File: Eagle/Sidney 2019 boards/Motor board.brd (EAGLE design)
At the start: 110 x 122 mm, 43 parts, among them IC2 LM2940CS-5.0_NOPB, IC3 LM3940IS-3.3

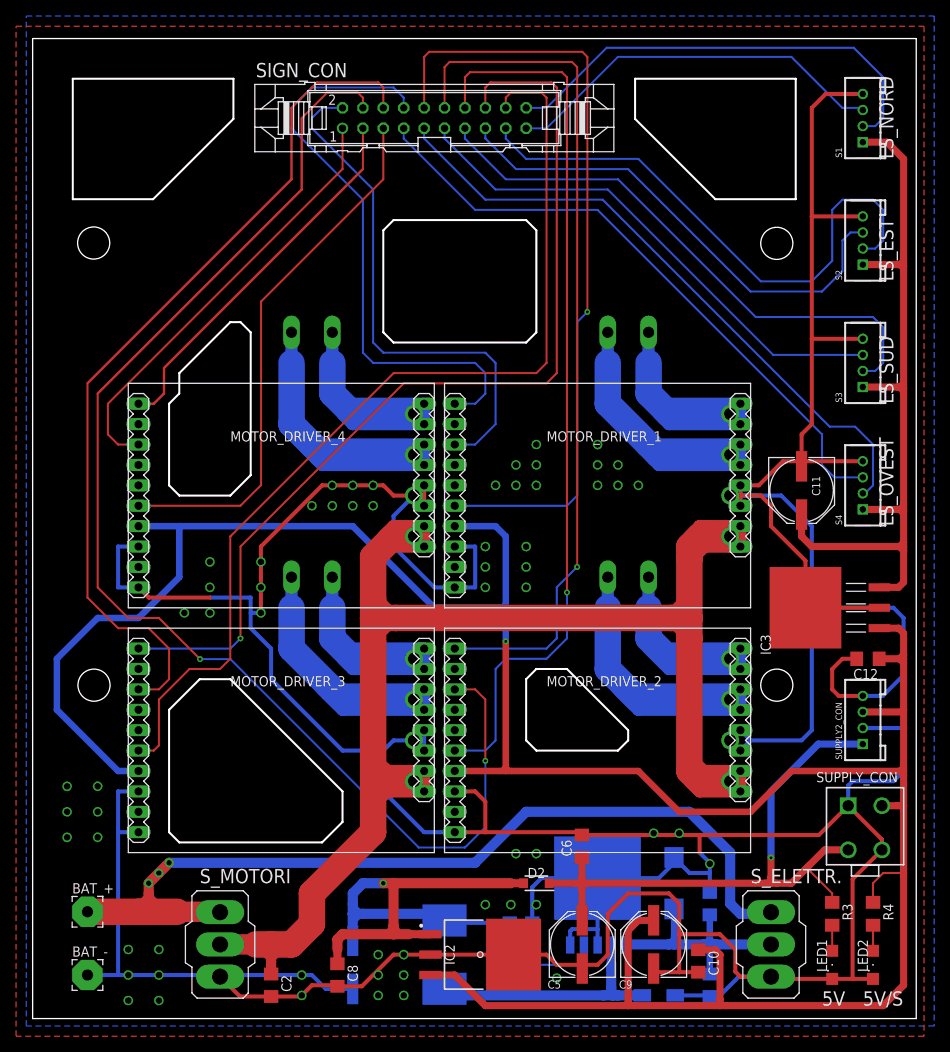
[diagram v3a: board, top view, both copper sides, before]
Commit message: Fixed motor driver pin hardly connected to ground
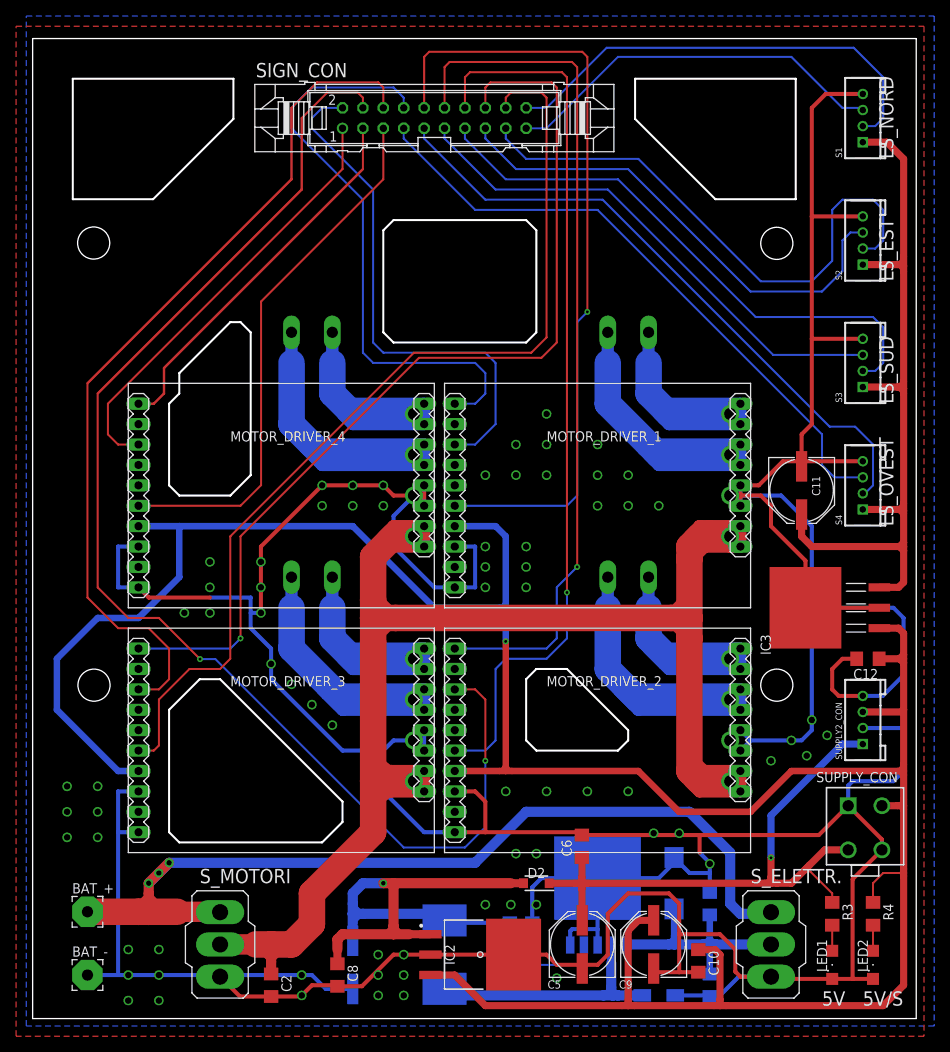
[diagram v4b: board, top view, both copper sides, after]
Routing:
- net M3_INB: track 123.0 -> 121.1 mm
- net +5V: track 85.8 -> 84.0 mm
- net M3_INA: track 120.5 -> 119.0 mm
- net GND: vias 61 -> 73
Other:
- outline, holes or cut-outs redrawn
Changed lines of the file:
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@@
 <wire x1="48.26" y1="74.93" x2="66.04" y2="74.93" width="0.254" layer="20"/>
 <wire x1="66.04" y1="74.93" x2="68.58" y2="77.47" width="0.254" layer="20"/>
-<wire x1="68.58" y1="77.47" x2="68.58" y2="81.28" width="0.254" layer="20"/>
-<wire x1="54.61" y1="95.25" x2="50.8" y2="95.25" width="0.254" layer="20"/>
+<wire x1="68.58" y1="77.47" x2="68.58" y2="80.01" width="0.254" layer="20"/>
+<wire x1="53.34" y1="95.25" x2="50.8" y2="95.25" width="0.254" layer="20"/>
 <wire x1="50.8" y1="95.25" x2="46.99" y2="91.44" width="0.254" layer="20"/>
 <wire x1="91.44" y1="95.25" x2="92.71" y2="96.52" width="0.254" layer="20"/>
@@
 <wire x1="46.99" y1="129.54" x2="46.99" y2="119.38" width="0.254" layer="20"/>
 <wire x1="46.99" y1="119.38" x2="48.26" y2="118.11" width="0.254" layer="20"/>
-<wire x1="54.61" y1="95.25" x2="68.58" y2="81.28" width="0.254" layer="20"/>
+<wire x1="53.34" y1="95.25" x2="68.58" y2="80.01" width="0.254" layer="20"/>
 </plain>
 <attributes>
@@
 <wire x1="43.18" y1="106.68" x2="44.45" y2="105.41" width="0.508" layer="1"/>
 <wire x1="58.42" y1="111.76" x2="66.04" y2="119.38" width="0.508" layer="1"/>
-<wire x1="66.04" y1="119.38" x2="67.31" y2="119.38" width="0.508" layer="1"/>
-<wire x1="69.85" y1="119.38" x2="67.31" y2="119.38" width="0.508" layer="1"/>
+<wire x1="69.85" y1="119.38" x2="66.04" y2="119.38" width="0.508" layer="1"/>
 <wire x1="77.47" y1="118.11" x2="78.74" y2="119.38" width="0.508" layer="1"/>
 <wire x1="78.74" y1="119.38" x2="78.74" y2="116.84" width="0.508" layer="1"/>
@@
 <via x="58.42" y="109.855" extent="1-16" drill="0.8"/>
 <via x="58.42" y="103.505" extent="1-16" drill="0.8"/>
-<via x="64.77" y="116.84" extent="1-16" drill="0.8"/>
-<via x="67.31" y="116.84" extent="1-16" drill="0.8"/>
+<via x="66.04" y="116.84" extent="1-16" drill="0.8"/>
 <via x="69.85" y="116.84" extent="1-16" drill="0.8"/>
-<via x="67.31" y="119.38" extent="1-16" drill="0.8"/>
+<via x="66.04" y="119.38" extent="1-16" drill="0.8"/>
 <via x="69.85" y="119.38" extent="1-16" drill="0.8"/>
-<via x="72.39" y="119.38" extent="1-16" drill="0.8"/>
+<via x="73.66" y="119.38" extent="1-16" drill="0.8"/>
 <wire x1="132.585" y1="97.79" x2="130.81" y2="97.79" width="0.508" layer="1"/>
 <wire x1="130.81" y1="97.79" x2="129.54" y2="96.52" width="0.508" layer="1"/>
@@
 <wire x1="100.33" y1="59.69" x2="101.6" y2="60.96" width="0.508" layer="1"/>
 <wire x1="101.6" y1="60.96" x2="101.6" y2="66.04" width="0.508" layer="1"/>
-<via x="90.17" y="119.38" extent="1-16" drill="0.8"/>
-<via x="87.63" y="119.38" extent="1-16" drill="0.8"/>
-<via x="92.71" y="119.38" extent="1-16" drill="0.8"/>
-<via x="90.17" y="121.92" extent="1-16" drill="0.8"/>
-<via x="92.71" y="121.92" extent="1-16" drill="0.8"/>
-<via x="92.71" y="124.46" extent="1-16" drill="0.8"/>
-<via x="105.41" y="119.38" extent="1-16" drill="0.8"/>
-<via x="102.87" y="119.38" extent="1-16" drill="0.8"/>
-<via x="100.33" y="119.38" extent="1-16" drill="0.8"/>
-<via x="100.33" y="121.92" extent="1-16" drill="0.8"/>
+<via x="90.17" y="124.46" extent="1-16" drill="0.8"/>
+<via x="86.36" y="120.65" extent="1-16" drill="0.8"/>
+<via x="93.98" y="120.65" extent="1-16" drill="0.8"/>
+<via x="90.17" y="120.65" extent="1-16" drill="0.8"/>
+<via x="93.98" y="128.27" extent="1-16" drill="0.8"/>
+<via x="93.98" y="124.46" extent="1-16" drill="0.8"/>
+<via x="107.95" y="116.84" extent="1-16" drill="0.8"/>
+<via x="104.14" y="116.84" extent="1-16" drill="0.8"/>
+<via x="100.33" y="116.84" extent="1-16" drill="0.8"/>
+<via x="100.33" y="120.65" extent="1-16" drill="0.8"/>
 <via x="100.33" y="124.46" extent="1-16" drill="0.8"/>
-<via x="102.87" y="121.92" extent="1-16" drill="0.8"/>
-<via x="72.39" y="116.84" extent="1-16" drill="0.8"/>
+<via x="104.14" y="120.65" extent="1-16" drill="0.8"/>
+<via x="73.66" y="116.84" extent="1-16" drill="0.8"/>
 <wire x1="125.73" y1="125.73" x2="125.73" y2="122.428" width="0.508" layer="1"/>
 <wire x1="125.73" y1="122.428" x2="125.778" y2="122.38" width="0.508" layer="1"/>
@@
 <via x="91.44" y="109.22" extent="1-16" drill="0.8"/>
 <via x="91.44" y="106.68" extent="1-16" drill="0.8"/>
-<wire x1="69.85" y1="119.38" x2="72.39" y2="119.38" width="0.508" layer="1"/>
-<wire x1="72.39" y1="119.38" x2="73.66" y2="119.38" width="0.508" layer="1"/>
+<wire x1="69.85" y1="119.38" x2="73.66" y2="119.38" width="0.508" layer="1"/>
 <wire x1="73.66" y1="119.38" x2="74.93" y2="118.11" width="0.508" layer="1"/>
 <wire x1="74.93" y1="118.11" x2="77.47" y2="118.11" width="0.508" layer="1"/>
@@
 <via x="107.315" y="76.073" extent="1-16" drill="0.8"/>
 <via x="110.49" y="76.073" extent="1-16" drill="0.8"/>
+<via x="67.31" y="89.535" extent="1-16" drill="0.8"/>
+<via x="64.77" y="92.075" extent="1-16" drill="0.8"/>
+<via x="62.23" y="94.615" extent="1-16" drill="0.8"/>
+<via x="59.69" y="97.155" extent="1-16" drill="0.8"/>
+<via x="88.9" y="81.28" extent="1-16" drill="0.8"/>
+<via x="93.98" y="81.28" extent="1-16" drill="0.8"/>
+<via x="99.06" y="81.28" extent="1-16" drill="0.8"/>
+<via x="104.14" y="81.28" extent="1-16" drill="0.8"/>
+<via x="121.92" y="85.09" extent="1-16" drill="0.8"/>
+<via x="124.46" y="87.63" extent="1-16" drill="0.8"/>
+<via x="127" y="90.17" extent="1-16" drill="0.8"/>
+<via x="126.365" y="85.725" extent="1-16" drill="0.8"/>
+<via x="128.905" y="88.265" extent="1-16" drill="0.8"/>
 </signal>
 <signal name="+5V">
@@
 <wire x1="97.61941875" y1="69.85" x2="98.38141875" y2="70.612" width="0.3048" layer="1"/>
 <contactref element="SUPPLY2_CON" pad="1"/>
-<wire x1="133.35" y1="87.17" x2="127.81" y2="87.17" width="0.889" layer="16"/>
-<wire x1="121.92" y1="81.28" x2="121.92" y2="73.025" width="0.889" layer="16"/>
+<wire x1="133.35" y1="87.17" x2="130.81" y2="87.17" width="0.889" layer="16"/>
 <via x="121.92" y="73.025" extent="1-16" drill="0.35"/>
 <wire x1="121.92" y1="73.025" x2="121.92" y2="70.612" width="0.889" layer="1"/>
@@
 <wire x1="121.158" y1="69.85" x2="121.92" y2="70.612" width="0.4064" layer="1"/>
 <wire x1="121.92" y1="70.612" x2="122.682" y2="69.85" width="0.4064" layer="1"/>
-<wire x1="127.81" y1="87.17" x2="121.92" y2="81.28" width="0.889" layer="16"/>
+<wire x1="130.81" y1="87.17" x2="121.92" y2="78.28" width="0.889" layer="16"/>
+<wire x1="121.92" y1="78.28" x2="121.92" y2="73.025" width="0.889" layer="16"/>
 </signal>
 <signal name="N$6">
@@
 <wire x1="63.5" y1="165.1" x2="63.5" y2="156.21" width="0.3048" layer="1"/>
 <wire x1="63.5" y1="156.21" x2="38.1" y2="130.81" width="0.3048" layer="1"/>
-<wire x1="50.84" y1="97.75" x2="54.61" y2="97.75" width="0.254" layer="16"/>
-<wire x1="54.61" y1="97.75" x2="78.065" y2="74.295" width="0.254" layer="16"/>
-<wire x1="78.065" y1="74.295" x2="83.82" y2="74.295" width="0.254" layer="16"/>
+<wire x1="50.84" y1="97.75" x2="52.745" y2="97.75" width="0.254" layer="16"/>
+<wire x1="76.2" y1="74.295" x2="83.82" y2="74.295" width="0.254" layer="16"/>
+<wire x1="76.2" y1="74.295" x2="52.745" y2="97.75" width="0.254" layer="16"/>
 </signal>
 <signal name="M2_INA">
@@
 <wire x1="86.36" y1="166.37" x2="86.36" y2="168.91" width="0.254" layer="1"/>
 <wire x1="86.36" y1="168.91" x2="86.995" y2="169.545" width="0.254" layer="1"/>
-<wire x1="55.88" y1="111.76" x2="55.88" y2="100.33" width="0.254" layer="1"/>
 <via x="55.88" y="100.33" extent="1-16" drill="0.35"/>
 <wire x1="55.88" y1="100.33" x2="54.61" y2="99.06" width="0.254" layer="16"/>
-<wire x1="76.2" y1="132.08" x2="55.88" y2="111.76" width="0.254" layer="1"/>
-<wire x1="95.25" y1="133.35" x2="93.98" y2="132.08" width="0.254" layer="1"/>
-<wire x1="93.98" y1="132.08" x2="76.2" y2="132.08" width="0.254" layer="1"/>
-<wire x1="95.25" y1="168.91" x2="95.25" y2="133.35" width="0.254" layer="1"/>
+<wire x1="95.25" y1="168.91" x2="95.25" y2="137.16" width="0.254" layer="1"/>
+<wire x1="95.25" y1="137.16" x2="93.345" y2="135.255" width="0.254" layer="1"/>
+<wire x1="93.345" y1="135.255" x2="78.105" y2="135.255" width="0.254" layer="1"/>
+<wire x1="78.105" y1="135.255" x2="55.88" y2="113.03" width="0.254" layer="1"/>
+<wire x1="55.88" y1="113.03" x2="55.88" y2="100.33" width="0.254" layer="1"/>
 </signal>
 <signal name="M3_INB">
@@
 <wire x1="93.98" y1="167.64" x2="93.345" y2="168.275" width="0.254" layer="1"/>
 <wire x1="89.535" y1="168.275" x2="93.345" y2="168.275" width="0.254" layer="1"/>
-<wire x1="44.45" y1="86.36" x2="43.18" y2="86.36" width="0.254" layer="1"/>
-<wire x1="54.61" y1="113.03" x2="74.93" y2="133.35" width="0.254" layer="1"/>
-<wire x1="54.61" y1="113.03" x2="54.61" y2="97.79" width="0.254" layer="1"/>
-<wire x1="74.93" y1="133.35" x2="92.71" y2="133.35" width="0.254" layer="1"/>
-<wire x1="92.71" y1="133.35" x2="93.98" y2="134.62" width="0.254" layer="1"/>
-<wire x1="93.98" y1="134.62" x2="93.98" y2="167.64" width="0.254" layer="1"/>
+<wire x1="45.085" y1="86.36" x2="43.18" y2="86.36" width="0.254" layer="1"/>
+<wire x1="54.61" y1="97.79" x2="54.61" y2="113.03" width="0.254" layer="1"/>
+<wire x1="93.98" y1="137.795" x2="93.98" y2="167.64" width="0.254" layer="1"/>
 <wire x1="54.61" y1="97.79" x2="53.34" y2="96.52" width="0.254" layer="1"/>
 <wire x1="53.34" y1="96.52" x2="49.53" y2="96.52" width="0.254" layer="1"/>
 <wire x1="49.53" y1="96.52" x2="45.72" y2="92.71" width="0.254" layer="1"/>
 <wire x1="45.72" y1="86.995" x2="45.085" y2="86.36" width="0.254" layer="1"/>
-<wire x1="45.085" y1="86.36" x2="44.45" y2="86.36" width="0.254" layer="1"/>
 <wire x1="45.72" y1="92.71" x2="45.72" y2="86.995" width="0.254" layer="1"/>
+<wire x1="92.075" y1="135.89" x2="93.98" y2="137.795" width="0.254" layer="1"/>
+<wire x1="54.61" y1="113.03" x2="77.47" y2="135.89" width="0.254" layer="1"/>
+<wire x1="77.47" y1="135.89" x2="92.075" y2="135.89" width="0.254" layer="1"/>
 </signal>
 <signal name="M4_PWM">

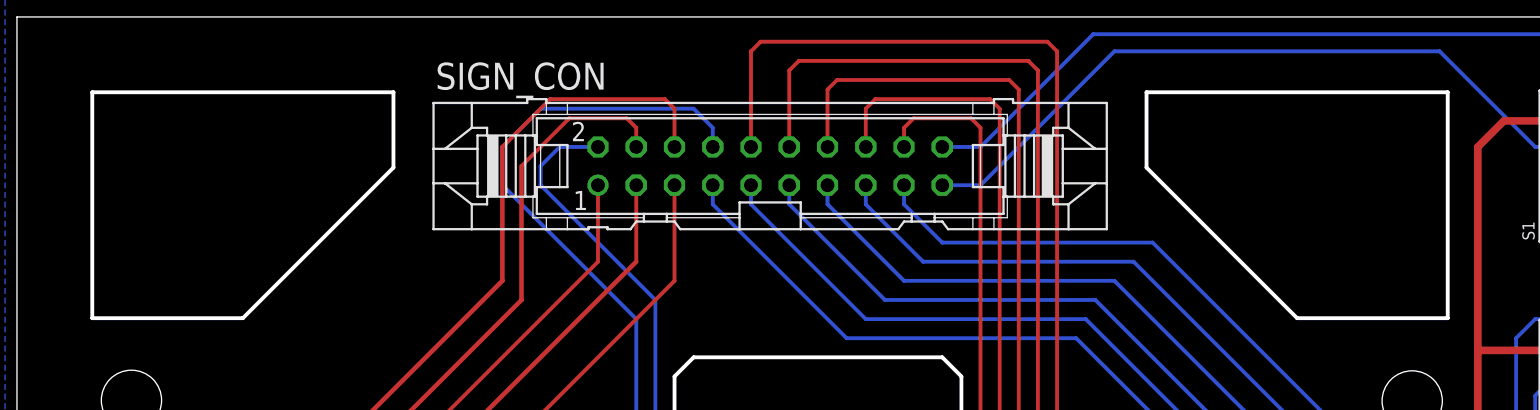
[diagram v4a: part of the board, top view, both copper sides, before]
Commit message: Created DXFs, PDFs and PNGs, small improvements to line sensors board
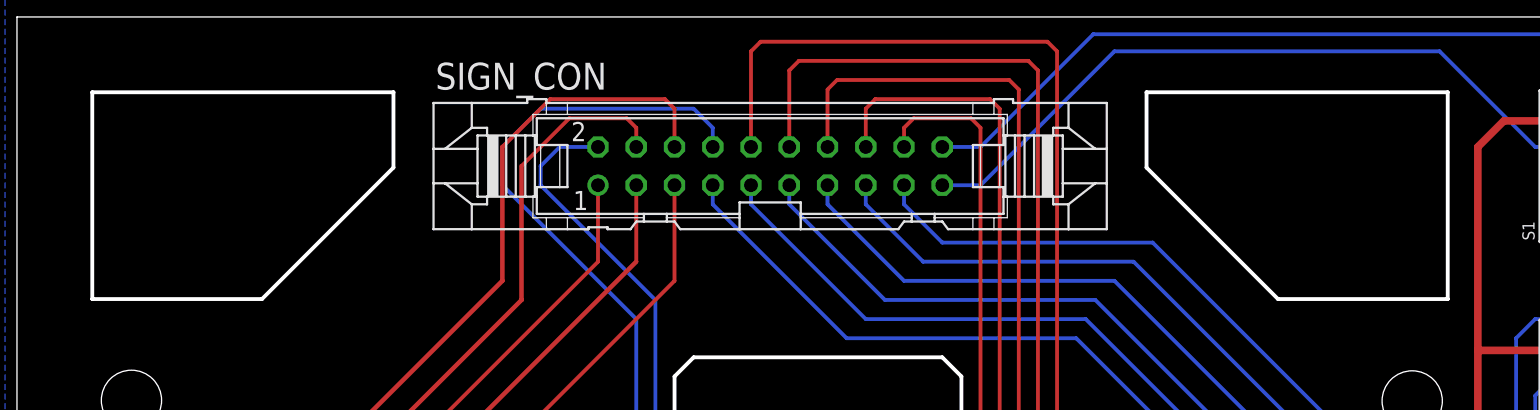
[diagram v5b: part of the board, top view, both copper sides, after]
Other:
- outline, holes or cut-outs redrawn
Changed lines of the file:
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@@
 <drawing>
 <settings>
-<setting alwaysvectorfont="yes"/>
+<setting alwaysvectorfont="no"/>
 <setting verticaltext="up"/>
 </settings>
@@
 <text x="137.16" y="129.54" size="1.778" layer="25" rot="R90">LS_SUD</text>
 <text x="137.16" y="114.3" size="1.778" layer="25" rot="R90">LS_OVEST</text>
-<wire x1="105" y1="165" x2="115" y2="155" width="0.254" layer="20"/>
-<wire x1="125" y1="155" x2="125" y2="170" width="0.254" layer="20"/>
+<wire x1="105" y1="165" x2="113.73" y2="156.27" width="0.254" layer="20"/>
+<wire x1="125" y1="156.27" x2="125" y2="170" width="0.254" layer="20"/>
 <wire x1="125" y1="170" x2="105" y2="170" width="0.254" layer="20"/>
 <wire x1="105" y1="170" x2="105" y2="165" width="0.254" layer="20"/>
 <wire x1="35" y1="170" x2="55" y2="170" width="0.254" layer="20"/>
 <wire x1="55" y1="170" x2="55" y2="165" width="0.254" layer="20"/>
-<wire x1="45" y1="155" x2="35" y2="155" width="0.254" layer="20"/>
-<wire x1="35" y1="155" x2="35" y2="170" width="0.254" layer="20"/>
-<wire x1="115" y1="155" x2="125" y2="155" width="0.254" layer="20"/>
-<wire x1="55" y1="165" x2="45" y2="155" width="0.254" layer="20"/>
+<wire x1="46.27" y1="156.27" x2="35" y2="156.27" width="0.254" layer="20"/>
+<wire x1="35" y1="156.27" x2="35" y2="170" width="0.254" layer="20"/>
+<wire x1="113.73" y1="156.27" x2="125" y2="156.27" width="0.254" layer="20"/>
+<wire x1="55" y1="165" x2="46.27" y2="156.27" width="0.254" layer="20"/>
 <wire x1="73.66" y1="138.43" x2="74.93" y2="137.16" width="0.254" layer="20"/>
 <wire x1="74.93" y1="137.16" x2="91.44" y2="137.16" width="0.254" layer="20"/>
